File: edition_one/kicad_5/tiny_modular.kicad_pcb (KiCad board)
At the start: 2 copper layers, 30 x 128.5 mm, 21 parts, among them J1 Conn_01x01, J2 Conn_01x01, J3 Conn_01x03, J4 Conn_01x06, J5 AudioJack2, J6 AudioJack2, J7 AudioJack2, J8 AudioJack2, SW1 SW_Push, U1 ATtiny85V-10SU

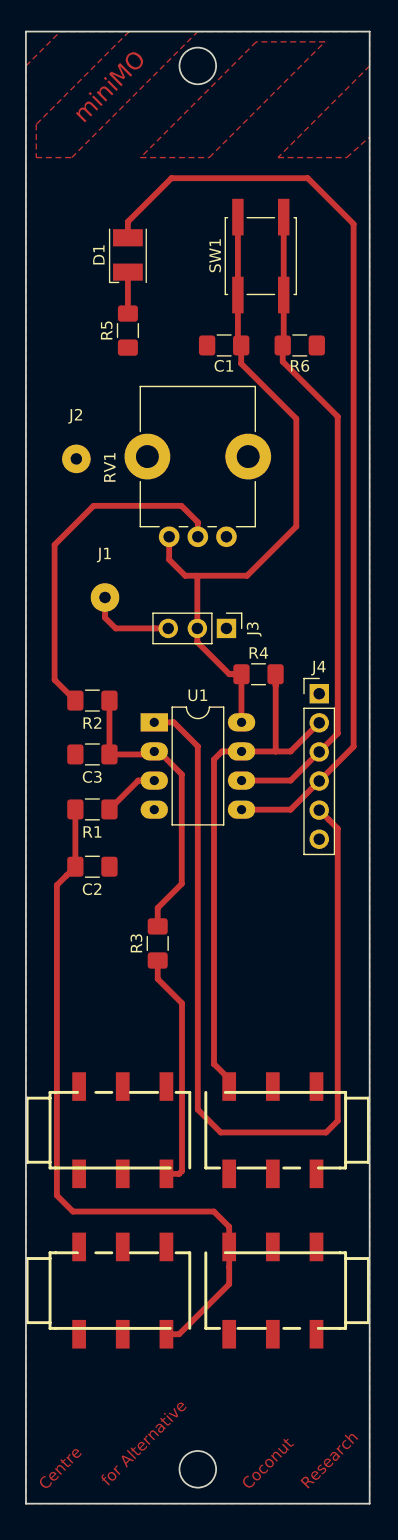
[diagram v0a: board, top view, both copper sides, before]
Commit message: Revision anyma 2019 with vertical jack sockets
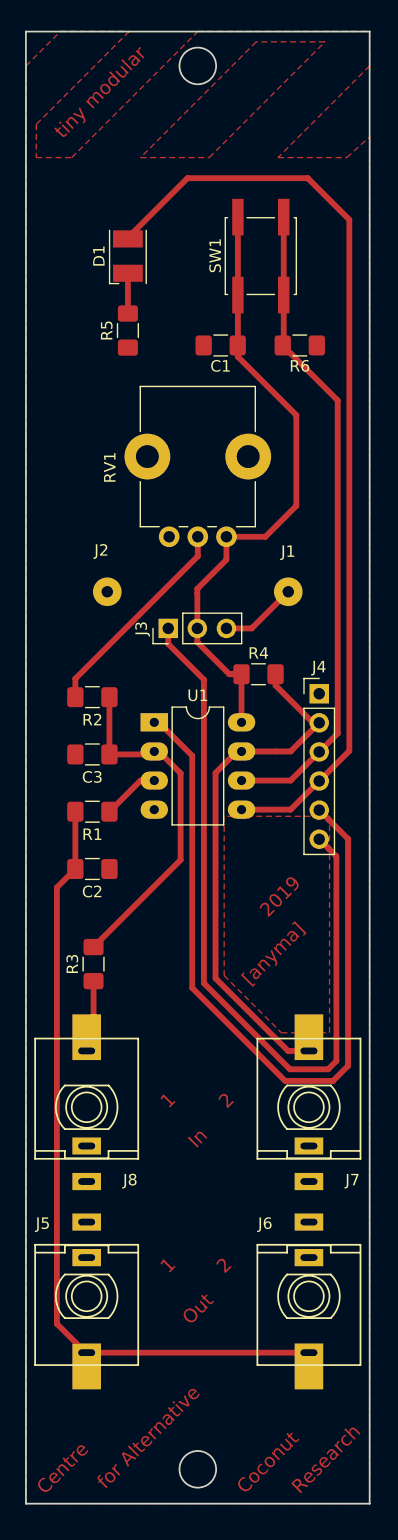
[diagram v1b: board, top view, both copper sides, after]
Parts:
- J5, J6, J7, J8: footprint Custom:AUDIO-JACK-3.5mm_SMD_noHole -> Custom:PJ301M-12_bent
- moved J1 16.0 mm to (66.0, 90.3)
- moved J2 12.0 mm to (49.7, 90.2)
- moved R3 5.88 mm to (49.0, 122.5)
- moved J3 5.08 mm to (55.5, 93.2), turned to 90 degrees
- moved J7 3.77 mm to (67.8, 135.0), turned to 0 degrees
- moved J8 3.77 mm to (48.4, 135.0)
- moved J6 3.24 mm to (67.8, 151.5)
- moved J5 3.24 mm to (48.4, 151.5), turned to 180 degrees
- moved C1 0.30 mm to (60.1, 68.5)
- moved R2 0.30 mm to (48.9, 99.2)
- moved C2 0.20 mm to (48.9, 114.2)
- moved R1 0.20 mm to (48.9, 109.2)
- moved D1 0.10 mm to (52.0, 60.7)
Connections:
- J5 pad 1: (no net) -> GND
- J5 pad 3: (no net) -> Net-(C2-Pad2)
- J6 pad 1: (no net) -> GND
- J6 pad 3: (no net) -> Net-(C2-Pad2)
- J7 pad 1: (no net) -> GND
- J7 pad 3: (no net) -> Net-(J4-Pad2)
- J8 pad 1: (no net) -> GND
- J8 pad 3: (no net) -> Net-(J8-Pad3)
- R3 pad 1: Net-(J8-PadT) -> Net-(J8-Pad3)
- RV1 pad 1: GND -> Net-(C1-Pad1)
- RV1 pad 3: Net-(C1-Pad1) -> GND
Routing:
- net Net-(J3-Pad1): track 0.00 -> 67.2 mm
- net Net-(J8-PadT): track 20.7 -> 0.00 mm
- net Net-(J4-Pad5): track 77.6 -> 65.7 mm
- net Net-(R2-Pad1): track 30.1 -> 18.4 mm
- net Net-(J8-Pad3): track 0.00 -> 7.09 mm
- net Net-(C2-Pad2): track 62.8 -> 68.4 mm
- net Net-(C1-Pad1): track 59.6 -> 54.1 mm
- net Net-(C3-Pad1): track 26.1 -> 30.4 mm
- net Net-(D1-Pad2): track 82.0 -> 80.9 mm
- net Net-(J1-Pad1): track 7.67 -> 6.73 mm
- net Net-(J4-Pad2): track 46.4 -> 45.7 mm
- added copper zone on F.Cu, net (none)
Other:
- board text added: "1"
- board text added: "2"
- board text added: "2019"
- board text added: "In"
- board text added: "Out"
- board text added: "[anyma]"
- board text added: "tiny modular"
- board text removed: "miniMO"
